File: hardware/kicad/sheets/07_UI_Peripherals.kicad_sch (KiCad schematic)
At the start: 17 parts, among them Q701 2N7002-class open-drain reset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, U701 3ch active-low panel encoder 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, U702 TCA9535-class, +3V3_CORE, add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, U703 4x 60 V logic NMOS; 100Ω gate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, U704 2.42-inch SSD1309 OLED refere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, U705 BME280 environmental sensor r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, U706 J6: 100 kHz; OLED_VCC-qualifi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, U707 J7: 100 kHz; SENSOR_VCC-quali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

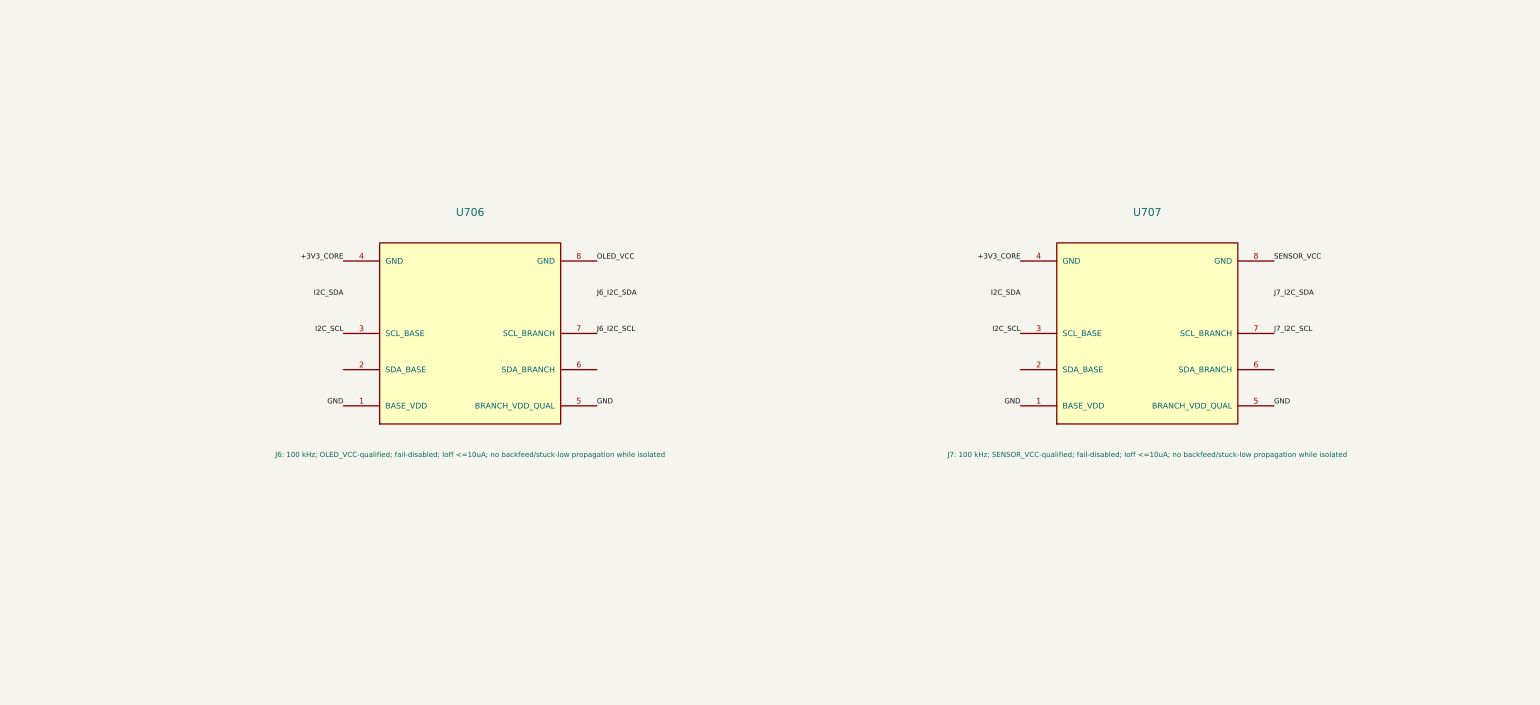
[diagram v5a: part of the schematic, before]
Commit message: Complete ECO-006 power compatibility remediation
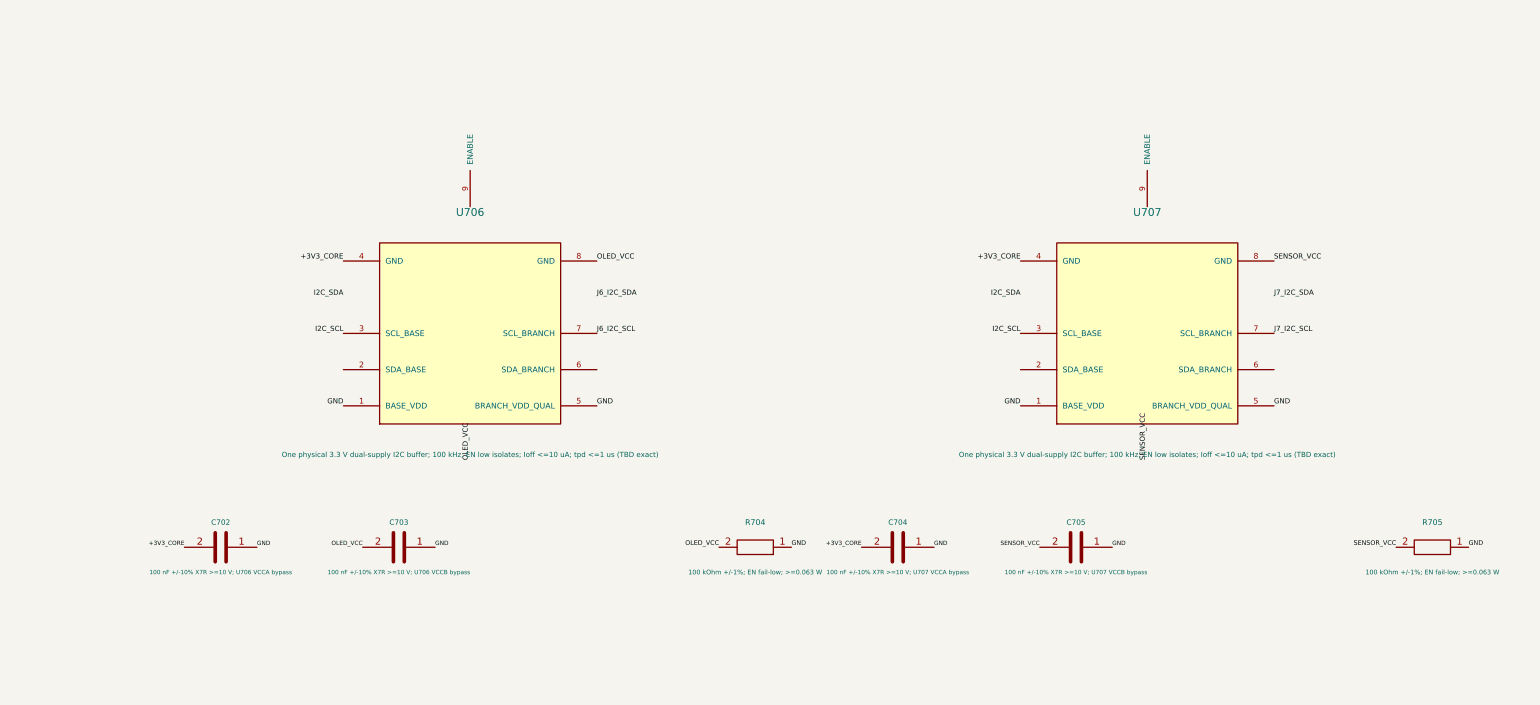
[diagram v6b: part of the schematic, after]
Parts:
- added C702: 100 nF +/-10% X7R >=10 V; U706 VCCA bypass, symbol IPC100:C
- added C703: 100 nF +/-10% X7R >=10 V; U706 VCCB bypass, symbol IPC100:C
- added C704: 100 nF +/-10% X7R >=10 V; U707 VCCA bypass, symbol IPC100:C
- added C705: 100 nF +/-10% X7R >=10 V; U707 VCCB bypass, symbol IPC100:C
- added R704, R705: 100 kOhm +/-1%; EN fail-low; >=0.063 W, symbol IPC100:R
- U706: value J6: 100 kHz; OLED_VCC-qualified; fail-disabled; Ioff <=10uA; no backfeed/stuck-low propagation while isolated -> One physical 3.3 V dual-supply I2C buffer; 100 kHz; EN low isolates; Ioff <=10 uA; tpd <=1 us (TBD exact); symbol IPC100:I2C_POWER_QUALIFIED_BRANCH -> IPC100:I2C_DUAL_SUPPLY_BUFFER_EN
- U707: value J7: 100 kHz; SENSOR_VCC-qualified; fail-disabled; Ioff <=10uA; no backfeed/stuck-low propagation while isolated -> One physical 3.3 V dual-supply I2C buffer; 100 kHz; EN low isolates; Ioff <=10 uA; tpd <=1 us (TBD exact); symbol IPC100:I2C_POWER_QUALIFIED_BRANCH -> IPC100:I2C_DUAL_SUPPLY_BUFFER_EN
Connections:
- net +3V3_CORE: now also C702.2, C704.2
- net GND: now also C702.1, C703.1, C704.1, C705.1, R704.1, R705.1
- net OLED_VCC: now also C703.2, R704.2
- net SENSOR_VCC: now also C705.2, R705.2
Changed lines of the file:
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@@
   (no_connect (at 274.76 162.62))
   (label "GND" (at 305.24 162.62 0) (effects (font (size 0.85 0.85)) (justify left bottom)))
-  (symbol (lib_id "IPC100:I2C_POWER_QUALIFIED_BRANCH") (at 380 150 0) (unit 1) (exclude_from_sim no) (in_bom yes) (on_board yes) (dnp no)
+  (symbol (lib_id "IPC100:I2C_DUAL_SUPPLY_BUFFER_EN") (at 380 150 0) (unit 1) (exclude_from_sim no) (in_bom yes) (on_board yes) (dnp no)
     (property "Reference" "U706" (at 380 133 0) (effects (font (size 1.1 1.1))))
-    (property "Value" "J6: 100 kHz; OLED_VCC-qualified; fail-disabled; Ioff <=10uA; no backfeed/stuck-low propagation while isolated" (at 380 167 0) (effects (font (size 0.72 0.72))))
+    (property "Value" "One physical 3.3 V dual-supply I2C buffer; 100 kHz; EN low isolates; Ioff <=10 uA; tpd <=1 us (TBD exact)" (at 380 167 0) (effects (font (size 0.72 0.72))))
     (property "Footprint" "" (at 380 150 0) (effects (font (size 1 1)) hide)) (property "Datasheet" "" (at 380 150 0) (effects (font (size 1 1)) hide))
-    (pin "1") (pin "2") (pin "3") (pin "4") (pin "5") (pin "6") (pin "7") (pin "8")
+    (pin "1") (pin "2") (pin "3") (pin "4") (pin "5") (pin "6") (pin "7") (pin "8") (pin "9")
     (instances (project "IPC-100" (path "/10000000-0000-4000-8000-000000000001/10000000-0000-4000-8000-000000000365" (reference "U706") (unit 1))))
   )
@@
   (label "J6_I2C_SCL" (at 397.78 150 0) (effects (font (size .72 .72)) (justify left bottom)))
   (label "GND" (at 397.78 160.16 0) (effects (font (size .72 .72)) (justify left bottom)))
-  (symbol (lib_id "IPC100:I2C_POWER_QUALIFIED_BRANCH") (at 475 150 0) (unit 1) (exclude_from_sim no) (in_bom yes) (on_board yes) (dnp no)
+  (label "OLED_VCC" (at 380 167.78 90) (effects (font (size .72 .72)) (justify left bottom)))
+  (symbol (lib_id "IPC100:I2C_DUAL_SUPPLY_BUFFER_EN") (at 475 150 0) (unit 1) (exclude_from_sim no) (in_bom yes) (on_board yes) (dnp no)
     (property "Reference" "U707" (at 475 133 0) (effects (font (size 1.1 1.1))))
-    (property "Value" "J7: 100 kHz; SENSOR_VCC-qualified; fail-disabled; Ioff <=10uA; no backfeed/stuck-low propagation while isolated" (at 475 167 0) (effects (font (size 0.72 0.72))))
+    (property "Value" "One physical 3.3 V dual-supply I2C buffer; 100 kHz; EN low isolates; Ioff <=10 uA; tpd <=1 us (TBD exact)" (at 475 167 0) (effects (font (size 0.72 0.72))))
     (property "Footprint" "" (at 475 150 0) (effects (font (size 1 1)) hide)) (property "Datasheet" "" (at 475 150 0) (effects (font (size 1 1)) hide))
-    (pin "1") (pin "2") (pin "3") (pin "4") (pin "5") (pin "6") (pin "7") (pin "8")
+    (pin "1") (pin "2") (pin "3") (pin "4") (pin "5") (pin "6") (pin "7") (pin "8") (pin "9")
     (instances (project "IPC-100" (path "/10000000-0000-4000-8000-000000000001/10000000-0000-4000-8000-000000000365" (reference "U707") (unit 1))))
   )
@@
   (label "J7_I2C_SCL" (at 492.78 150 0) (effects (font (size .72 .72)) (justify left bottom)))
   (label "GND" (at 492.78 160.16 0) (effects (font (size .72 .72)) (justify left bottom)))
+  (label "SENSOR_VCC" (at 475 167.78 90) (effects (font (size .72 .72)) (justify left bottom)))
+  (symbol (lib_id "IPC100:R") (at 420 180 90) (unit 1) (exclude_from_sim no) (in_bom yes) (on_board yes) (dnp no)
+ (property "Reference" "R704" (at 420 176.5 90) (effects (font (size .8 .8)))) (property "Value" "100 kOhm +/-1%; EN fail-low; >=0.063 W" (at 420 183.5 90) (effects (font (size .65 .65)))) (property "Footprint" "" (at 420 180 0) (effects (font (size 1 1)) hide)) (property "Datasheet" "" (at 420 180 0) (effects (font (size 1 1)) hide)) (pin "1") (pin "2") (instances (project "IPC-100" (path "/10000000-0000-4000-8000-000000000001/10000000-0000-4000-8000-000000000365" (reference "R704") (unit 1)))))
+  (label "OLED_VCC" (at 414.92 180 180) (effects (font (size .65 .65)) (justify right bottom)))
+  (label "GND" (at 425.08 180 0) (effects (font (size .65 .65)) (justify left bottom)))
+  (symbol (lib_id "IPC100:R") (at 515 180 90) (unit 1) (exclude_from_sim no) (in_bom yes) (on_board yes) (dnp no)
+ (property "Reference" "R705" (at 515 176.5 90) (effects (font (size .8 .8)))) (property "Value" "100 kOhm +/-1%; EN fail-low; >=0.063 W" (at 515 183.5 90) (effects (font (size .65 .65)))) (property "Footprint" "" (at 515 180 0) (effects (font (size 1 1)) hide)) (property "Datasheet" "" (at 515 180 0) (effects (font (size 1 1)) hide)) (pin "1") (pin "2") (instances (project "IPC-100" (path "/10000000-0000-4000-8000-000000000001/10000000-0000-4000-8000-000000000365" (reference "R705") (unit 1)))))
+  (label "SENSOR_VCC" (at 509.92 180 180) (effects (font (size .65 .65)) (justify right bottom)))
+  (label "GND" (at 520.08 180 0) (effects (font (size .65 .65)) (justify left bottom)))
+  (symbol (lib_id "IPC100:C") (at 345 180 90) (unit 1) (exclude_from_sim no) (in_bom yes) (on_board yes) (dnp no)
+ (property "Reference" "C702" (at 345 176.5 90) (effects (font (size .75 .75)))) (property "Value" "100 nF +/-10% X7R >=10 V; U706 VCCA bypass" (at 345 183.5 90) (effects (font (size .6 .6)))) (property "Footprint" "" (at 345 180 0) (effects (font (size 1 1)) hide)) (property "Datasheet" "" (at 345 180 0) (effects (font (size 1 1)) hide)) (pin "1") (pin "2") (instances (project "IPC-100" (path "/10000000-0000-4000-8000-000000000001/10000000-0000-4000-8000-000000000365" (reference "C702") (unit 1)))))
+  (label "+3V3_CORE" (at 339.92 180 180) (effects (font (size .6 .6)) (justify right bottom))) (label "GND" (at 350.08 180 0) (effects (font (size .6 .6)) (justify left bottom)))
+  (symbol (lib_id "IPC100:C") (at 370 180 90) (unit 1) (exclude_from_sim no) (in_bom yes) (on_board yes) (dnp no)
+ (property "Reference" "C703" (at 370 176.5 90) (effects (font (size .75 .75)))) (property "Value" "100 nF +/-10% X7R >=10 V; U706 VCCB bypass" (at 370 183.5 90) (effects (font (size .6 .6)))) (property "Footprint" "" (at 370 180 0) (effects (font (size 1 1)) hide)) (property "Datasheet" "" (at 370 180 0) (effects (font (size 1 1)) hide)) (pin "1") (pin "2") (instances (project "IPC-100" (path "/10000000-0000-4000-8000-000000000001/10000000-0000-4000-8000-000000000365" (reference "C703") (unit 1)))))
+  (label "OLED_VCC" (at 364.92 180 180) (effects (font (size .6 .6)) (justify right bottom))) (label "GND" (at 375.08 180 0) (effects (font (size .6 .6)) (justify left bottom)))
+  (symbol (lib_id "IPC100:C") (at 440 180 90) (unit 1) (exclude_from_sim no) (in_bom yes) (on_board yes) (dnp no)
+ (property "Reference" "C704" (at 440 176.5 90) (effects (font (size .75 .75)))) (property "Value" "100 nF +/-10% X7R >=10 V; U707 VCCA bypass" (at 440 183.5 90) (effects (font (size .6 .6)))) (property "Footprint" "" (at 440 180 0) (effects (font (size 1 1)) hide)) (property "Datasheet" "" (at 440 180 0) (effects (font (size 1 1)) hide)) (pin "1") (pin "2") (instances (project "IPC-100" (path "/10000000-0000-4000-8000-000000000001/10000000-0000-4000-8000-000000000365" (reference "C704") (unit 1)))))
+  (label "+3V3_CORE" (at 434.92 180 180) (effects (font (size .6 .6)) (justify right bottom))) (label "GND" (at 445.08 180 0) (effects (font (size .6 .6)) (justify left bottom)))
+  (symbol (lib_id "IPC100:C") (at 465 180 90) (unit 1) (exclude_from_sim no) (in_bom yes) (on_board yes) (dnp no)
+ (property "Reference" "C705" (at 465 176.5 90) (effects (font (size .75 .75)))) (property "Value" "100 nF +/-10% X7R >=10 V; U707 VCCB bypass" (at 465 183.5 90) (effects (font (size .6 .6)))) (property "Footprint" "" (at 465 180 0) (effects (font (size 1 1)) hide)) (property "Datasheet" "" (at 465 180 0) (effects (font (size 1 1)) hide)) (pin "1") (pin "2") (instances (project "IPC-100" (path "/10000000-0000-4000-8000-000000000001/10000000-0000-4000-8000-000000000365" (reference "C705") (unit 1)))))
+  (label "SENSOR_VCC" (at 459.92 180 180) (effects (font (size .6 .6)) (justify right bottom))) (label "GND" (at 470.08 180 0) (effects (font (size .6 .6)) (justify left bottom)))
   (text "OLED/SENSOR rails remain Sheet 02 controlled. U706/U707 qualify directly from their own branch rail and isolate before it is invalid. Sheet 07 remains sole owner of the 4.70k base-bus pull-up pair; no branch or Sheet 09 pull-ups." (at 20 180 0) (effects (font (size 0.82 0.82)) (justify left bottom)))
   (text "5 — SCHEMATIC DFT NODES (PHYSICAL PADS OWNED BY SHEET 09 / PCB DFT)" (at 20 200 0) (effects (font (size 1.15 1.15) (bold yes)) (justify left bottom)))
